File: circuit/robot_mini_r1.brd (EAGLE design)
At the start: 26 x 33 mm, 10 parts, among them M1 SERVO-FLIPPED, M2 SERVO-1, M3 SERVO-1, U1 ESP01

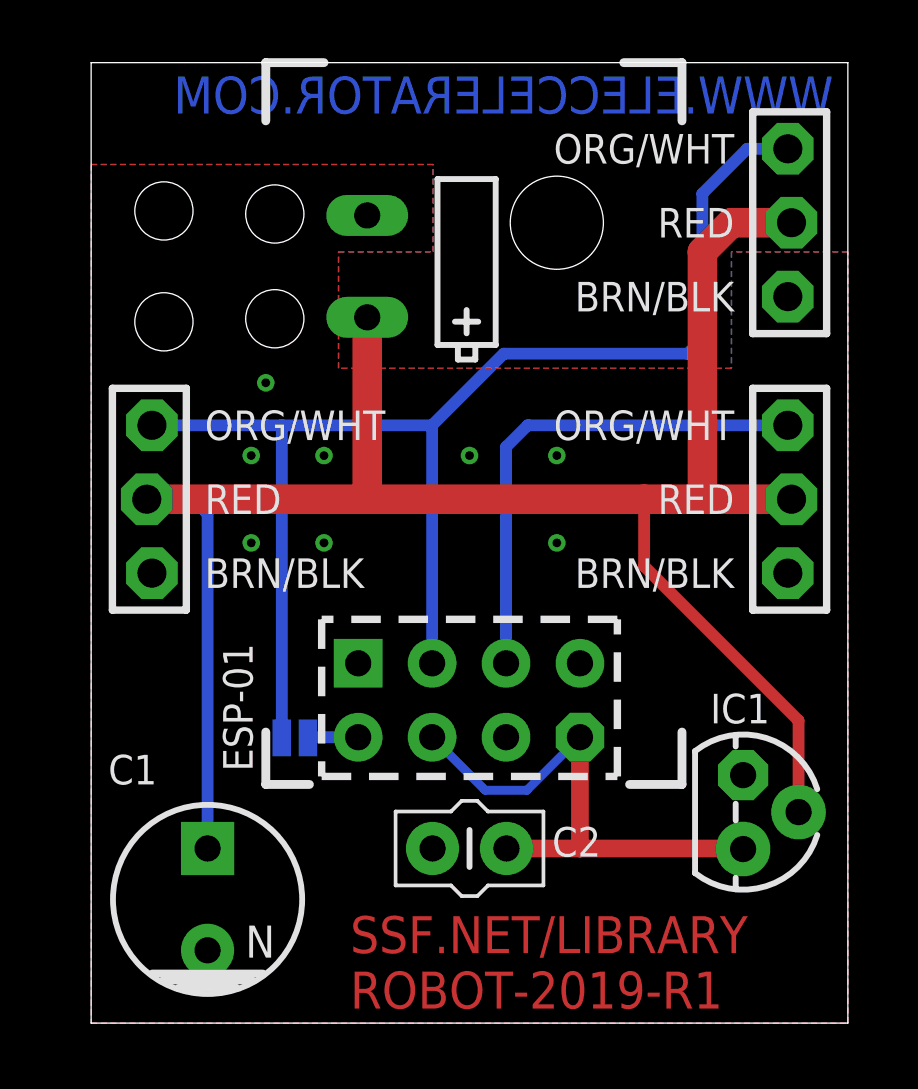
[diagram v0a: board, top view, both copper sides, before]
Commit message: web stuff works, more settings, PCB configurable
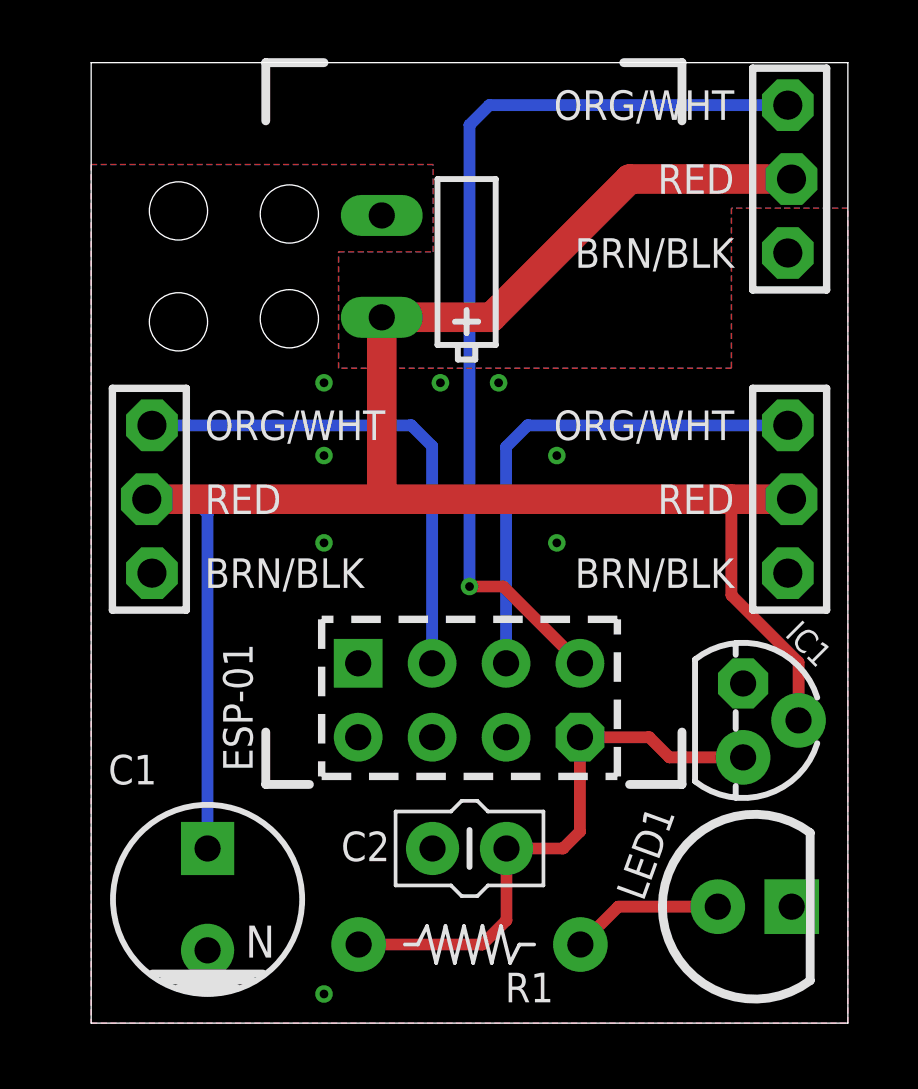
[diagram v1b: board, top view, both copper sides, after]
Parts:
- removed SJ1: (no value), robot:SJ_2S-NO
- added LED1: (no value), robot:LED5MM
- added R1: 220Ω, robot:AXIAL-0.3-NOVAL
- U$9: value TEXT-INFO-MINI -> TEXT-INFO-INVISIBLE; device robot:TEXT-INFO-MINI -> robot:TEXT-INFO-INVISIBLE
- moved U$9 18.1 mm to (27.0, 0.00)
- moved IC1 3.15 mm to (22.4, 10.4)
- moved M3 1.50 mm to (24.0, 29.0)
- moved BATTERY 0.50 mm to (3.00, 26.0)
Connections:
- removed net N$1: SJ1.2, U1.TX
- new net N$9: LED1.A, R1.P$2
- new net SERVO-AUX: M3.SIG, U1.RX
- net 3.3V: now also R1.P$1; no longer U1.CH_PD
- net GND: now also LED1.K
- net SERVO-LEFT: no longer M3.SIG, SJ1.1
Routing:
- net SERVO-AUX: track 0.00 -> 32.0 mm, vias 0 -> 1
- net SERVO-LEFT: track 47.6 -> 17.4 mm
- net N$9: track 0.00 -> 5.26 mm
- net N$1: track 1.75 -> 0.00 mm
- net 3.3V: track 18.6 -> 19.8 mm
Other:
- board text added: "SSF.NET/LIBRARY ROBOT-2019-REV1"
- board text removed: "WWW.ELECCELERATOR.COM"
